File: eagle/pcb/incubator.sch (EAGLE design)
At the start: 34 parts, among them IC1 MCP1703-50, IC2 MCP1703-50, J2 RJ12RIGHTANGLE-I2C, X2 8MHz, X4 MINI-USB

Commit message: routing in progress
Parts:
- removed BKLD1: RED, adafruit:LEDCHIP-LED0805
- removed C2: 10µF, microbuilder:CAP_CERAMIC0805
- removed C4: 100nF, dp_devices:CAPACITOR_NPOL-0805
- removed IC2: MCP1703-50, linear:MCP1703DB
- removed R7: 1k, rcl:R-EU_R0805
- removed RK1: 3.9k, rcl:R-EU_R0805
- added CX3, CX4: 1uF, rcl:C-EUC0805
- added D1: 1N581D1206, lpatiny:1N581D1206
- added J7: 22--02, lpatiny:22--02
- added JP1, JP2: (no value), SparkFun:JUMPER-2PTH
- added JP4, JP5: (no value), jumper:JP2E
- added POWER: JACK_DC_BARREL, lpatiny:JACK_DC_BARREL
- added Q1, Q5: BSP75, infineon:BSP613P
- added R1, R2: 1K, rcl:R-EU_R0805
- added R6: 10k, dp_devices:TRIMMER-3362P
- added RT1, RT2, RT3: 4.7k, resistor:R-EU_R0805
- added RXT1, RXT2, RXT3, RXT4, RXT5, RXT6, RXT7, RXT8: 10k, rcl:R-EU_R0805
- added U$3, U$4: BTS7960, BTS7960:BTS7960
- added U$5: DS18B20, lpatiny:DS18B20SMALL
- C10, C12, C13, CX1, CX2: device rcl:C-EUC1206 -> rcl:C-EUC0805
- RK3: value 100k -> 10k
- RUSB1, RUSB2: device resistor:R-EU_M1206 -> resistor:R-EU_M0805
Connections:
- removed net I2C+5V: D7.A, J2.5
- removed net VDD: CU7.1, IC1.VI
- new net +12V: CX3.2, CX4.2, D7.A, JP1.1, JP2.1, POWER.V+, U$3.VS, U$4.VS
- new net N$10: RXT2.2, U$4.SR
- new net N$13: RXT1.2, U$3.SR
- new net N$20: Q1.G, R2.2
- new net N$21: JP1.2, Q5.D@1
- new net N$22: J7-2.S, U$4.OUT
- new net N$23: JP2.2, Q1.D@1
- new net N$3: CU7.1, D1.C, D4.C, D7.C, D8.C, IC1.VI
- new net N$4: RXT5.1, U$3.IN
- new net N$5: RXT6.1, U$4.IN
- new net N$6: RXT4.1, U$3.INH
- new net N$7: RXT7.1, U$4.INH
- new net N$8: RXT3.1, U$4.IS
- new net N$9: Q5.G, R1.2
- net A0: now also R1.1
- net A1: now also R2.1
- net A2: now also RT2.2, U$5.DQ
- net A3: now also JP4.3, RT1.2
- net A4: now also JP5.3, RT3.2
- net A5: no longer R7.1
- net A6: no longer U$11.RS
- net D10*: now also U$11.DB6; no longer U$11.DB7
- net D11*: now also R6.3; no longer 220.1
- net D12*: now also U$11.RS; no longer U$11.E
- net D13*: now also 220.1; no longer RK1.1
- net D5*: now also U$11.DB7
- net D6*: now also U$11.E; no longer U$11.DB4
- net D8*: now also U$11.DB4; no longer U$11.DB5
- net D9*: now also U$11.DB5; no longer U$11.DB6
- net GND: now also CX3.1, CX4.1, JP4.2, JP5.2, POWER.GND, Q1.S, Q5.S, R6.1, RXT1.1, RXT2.1, RXT3.2, RXT8.2, U$3.GND, U$4.GND, U$5.GND; no longer BKLD1.C, C2.P$2, C4.2, IC2.GND
- net I2C+12V: now also D1.A; no longer IC2.VI
- net MISO: now also RXT4.2, RXT7.2
- net MOSI: now also RXT5.2; no longer U$11.VDD
- net N$14: now also RXT8.1, U$3.IS; no longer BKLD1.A, R7.2
- net N$19: now also J7-1.S, U$3.OUT; no longer C2.P$1, D4.C, D7.C, D8.C, IC2.VO
- net N$2: now also R6.2; no longer C4.1, RK1.2
- net SCK: now also RXT6.2
- net VCC: now also JP4.1, JP5.1, RT1.1, RT2.1, RT3.1, U$11.VDD, U$5.VDD
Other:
- note added: "5V LDO"
- note added: "One wire"
- note removed: "5.0V LDO"
- note removed: "RGB UV"
- moved on the sheet: 32U4, C10, C12, C13, CU1, CU7, CU8, CX1, CX2, D4, D7, D8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

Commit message: routing in progress
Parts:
- added D2: 1N581D1206, lpatiny:1N581D1206
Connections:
- removed net N$3: CU7.1, D1.C, D4.C, D7.C, D8.C, IC1.VI
- new net I2C+5V: D2.A, J2.5
- new net N$123: CU7.1, D1.C, D2.C, D4.C, D7.C, D8.C, IC1.VI

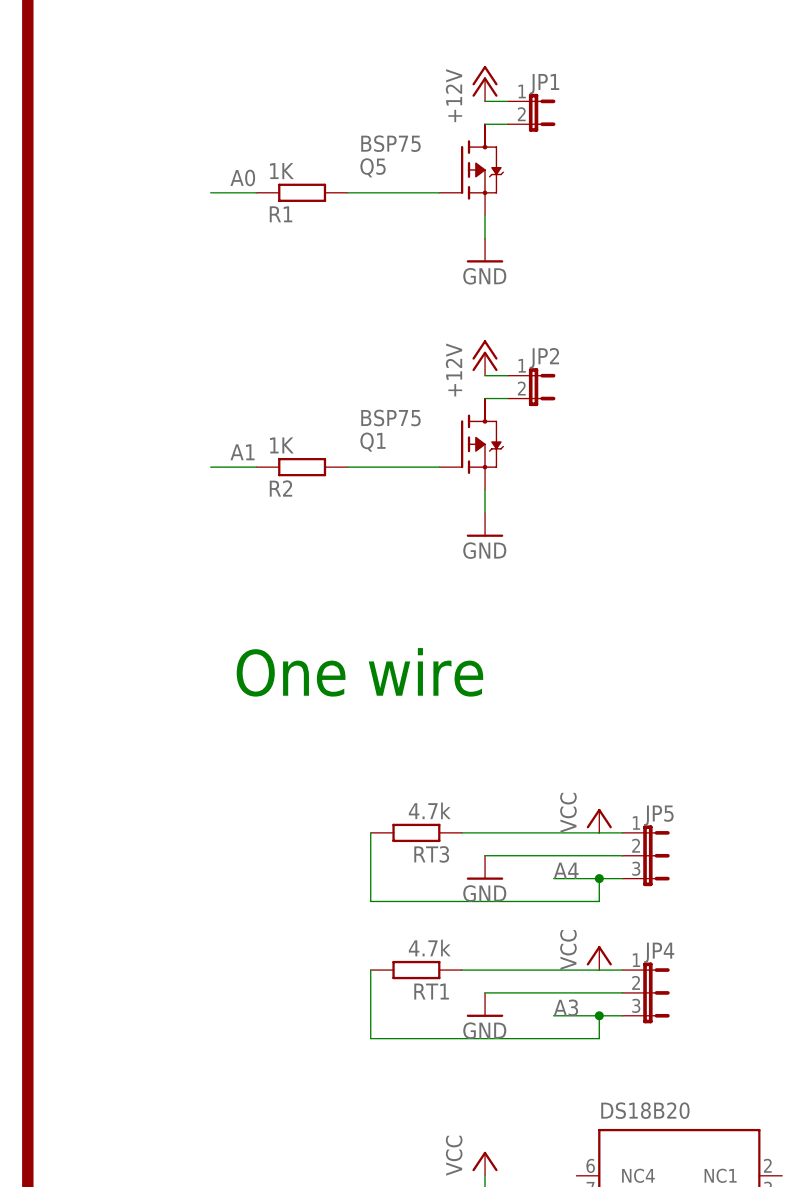
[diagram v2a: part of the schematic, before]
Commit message: first version of the incubator
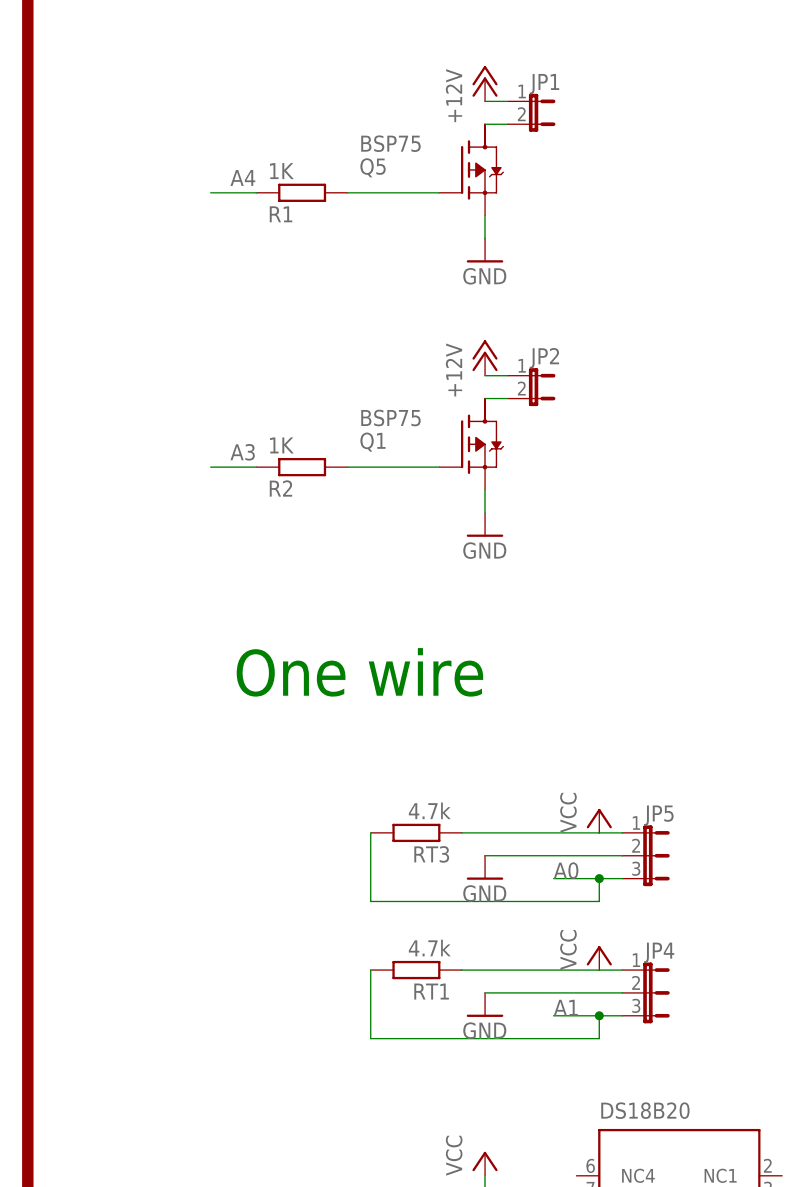
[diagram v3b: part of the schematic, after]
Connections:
- net A0: now also JP5.3, RT3.2; no longer R1.1
- net A1: now also JP4.3, RT1.2; no longer R2.1
- net A3: now also R2.1; no longer JP4.3, RT1.2
- net A4: now also R1.1; no longer JP5.3, RT3.2

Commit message: version 1.1
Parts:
- U$1: value EC11E -> ROTARYENCODER; device lpatiny:EC11E -> RotaryEncoder:ROTARYENCODER

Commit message: version 1.1.0
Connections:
- net A3: no longer R2.1
- net A4: no longer R1.1
- net A6: now also U$11.RS
- net D11*: now also R1.1; no longer R6.3
- net D12*: now also U$11.E; no longer U$11.RS
- net D6*: now also R2.1; no longer U$11.E
- net VCC: now also R6.3
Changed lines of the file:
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@@
 </segment>
 <segment>
-<wire x1="137.16" y1="55.88" x2="137.16" y2="58.42" width="0.1524" layer="91"/>
-<label x="134.62" y="58.42" size="1.778" layer="95"/>
-<pinref part="R6" gate="R" pin="3"/>
+<pinref part="R1" gate="G$1" pin="1"/>
+<wire x1="218.44" y1="185.42" x2="213.36" y2="185.42" width="0.1524" layer="91"/>
+<label x="218.44" y="187.96" size="1.778" layer="95" rot="R180"/>
 </segment>
 </net>
@@
 <label x="127" y="195.58" size="1.778" layer="95"/>
 </segment>
-<segment>
-<pinref part="R2" gate="G$1" pin="1"/>
-<wire x1="218.44" y1="154.94" x2="213.36" y2="154.94" width="0.1524" layer="91"/>
-<label x="218.44" y="157.48" size="1.778" layer="95" rot="R180"/>
-</segment>
 </net>
 <net name="A4" class="0">
@@
 <wire x1="116.84" y1="198.12" x2="132.08" y2="198.12" width="0.1524" layer="91"/>
 <label x="127" y="198.12" size="1.778" layer="95"/>
-</segment>
-<segment>
-<pinref part="R1" gate="G$1" pin="1"/>
-<wire x1="218.44" y1="185.42" x2="213.36" y2="185.42" width="0.1524" layer="91"/>
-<label x="218.44" y="187.96" size="1.778" layer="95" rot="R180"/>
 </segment>
 </net>
@@
 </segment>
 <segment>
-<wire x1="175.26" y1="43.18" x2="154.94" y2="43.18" width="0.1524" layer="91"/>
-<label x="154.94" y="43.18" size="1.778" layer="95"/>
-<pinref part="U$11" gate="G$1" pin="E"/>
-<junction x="175.26" y="43.18"/>
-<wire x1="175.26" y1="43.18" x2="167.64" y2="43.18" width="0.1524" layer="91"/>
+<pinref part="R2" gate="G$1" pin="1"/>
+<wire x1="218.44" y1="154.94" x2="213.36" y2="154.94" width="0.1524" layer="91"/>
+<label x="218.44" y="157.48" size="1.778" layer="95" rot="R180"/>
 </segment>
 </net>
@@
 </segment>
 <segment>
-<wire x1="175.26" y1="48.26" x2="154.94" y2="48.26" width="0.1524" layer="91"/>
-<label x="154.94" y="48.26" size="1.778" layer="95"/>
-<pinref part="U$11" gate="G$1" pin="RS"/>
-<junction x="175.26" y="48.26"/>
-<wire x1="175.26" y1="48.26" x2="167.64" y2="48.26" width="0.1524" layer="91"/>
+<wire x1="175.26" y1="43.18" x2="154.94" y2="43.18" width="0.1524" layer="91"/>
+<label x="154.94" y="43.18" size="1.778" layer="95"/>
+<pinref part="U$11" gate="G$1" pin="E"/>
+<junction x="175.26" y="43.18"/>
+<wire x1="175.26" y1="43.18" x2="167.64" y2="43.18" width="0.1524" layer="91"/>
 </segment>
 </net>
@@
 <label x="127" y="137.16" size="1.778" layer="95"/>
 </segment>
+<segment>
+<wire x1="175.26" y1="48.26" x2="154.94" y2="48.26" width="0.1524" layer="91"/>
+<label x="154.94" y="48.26" size="1.778" layer="95"/>
+<pinref part="U$11" gate="G$1" pin="RS"/>
+<junction x="175.26" y="48.26"/>
+<wire x1="175.26" y1="48.26" x2="167.64" y2="48.26" width="0.1524" layer="91"/>
+</segment>
 </net>
 <net name="N$2" class="0">
@@
 <label x="154.94" y="53.34" size="1.778" layer="95"/>
 <pinref part="P+6" gate="VCC" pin="VCC"/>
-</segment>
-</net>
+<wire x1="147.32" y1="53.34" x2="142.24" y2="53.34" width="0.1524" layer="91"/>
+<junction x="147.32" y="53.34"/>
+<wire x1="142.24" y1="53.34" x2="142.24" y2="55.88" width="0.1524" layer="91"/>
+<pinref part="R6" gate="R" pin="3"/>
+<wire x1="142.24" y1="55.88" x2="137.16" y2="55.88" width="0.1524" layer="91"/>
+</segment>
+</net>
